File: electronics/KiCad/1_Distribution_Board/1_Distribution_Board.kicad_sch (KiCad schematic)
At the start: 10 parts, among them Q1 DMG2305UX, SW1 SW_Push

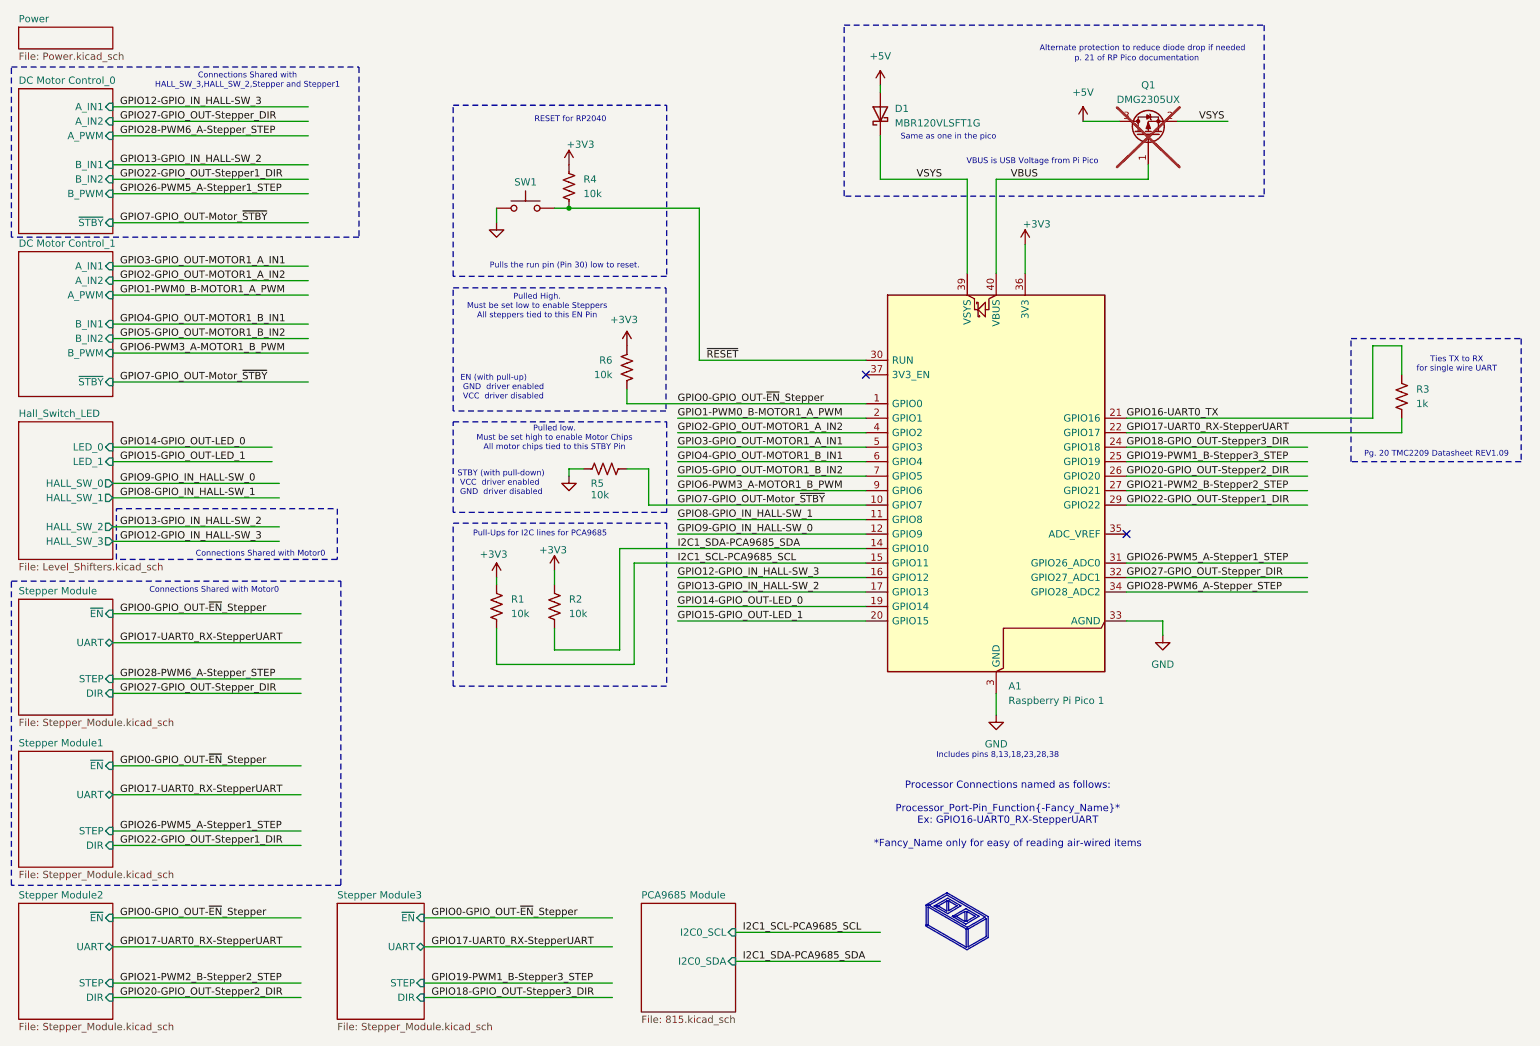
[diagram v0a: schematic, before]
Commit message: Merge board v1.3 into main (clean-clone fixups, generated files trimmed to main level) (#289)
* Initial start to updates

Removed motor pages, updated Q2,Q3, Cleaned up power module connections.

- Still need to correct routing for these updates.

* PCA Update

Updated PCA to have level shifter for I2C lines and external oscillator for precision. Corrected Power to pull from 12V.

* Removed old circuits from PCB

Removed all unused traces

* Mid work update

Lots of rework on the SCH and PCB. Checkpoint.

* Updated with more layout

Compelted PCA on board.

* adding libraries

* REV0.9 for review

Took care of all open items on the electronics PCB except for the driver resistor addresses.

* Updates Just prior to Ordering V1.0 PCBs

Updates Just prior to Ordering V1.0 PCBs

* Updates to push to V1.0

Updates to push to V1.0

* Updates to push to V1.0 missing saves. . .

Updates to push to V1.0 missing saves. . .

* Correcting Part rotation for JLCPCB

Several parts needed the "FT Rotation Offset" parameter added to correct for part orientation for JLCPCB order.

* All orientations corrected

* latest update

* Updated to reflect V1.0 of layer board as well

Updated for initial orders with PCA module populated. Also updated to layer boards for flex cables.

* Updated data and notes

* Corrected SCH for power sequence issue

5V to Vsys for all powered items.
Correction of the PCA9306 power pins.
Added decoupling to oscillator and PCA9306.

* Updated for changes to the SCH items

Updated PCB to include all changed from the SCH.

* Updated rules to correct errors

Cleaned up rules a bit to prevent false errors.

* Started work on silk update

Slowly started work on silk update.

* Corrected the 10k to 1k for connecting resistors

R1 got fixed for the correct 1k instead of 10k for UART1

* Updated Silk on PCB

Added notes for describing the pins better in the silk layer.

* Updated REV to 1.3 to reflect changes

* Updated with Version 1.3

* KiCad: make the v1.3 project 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
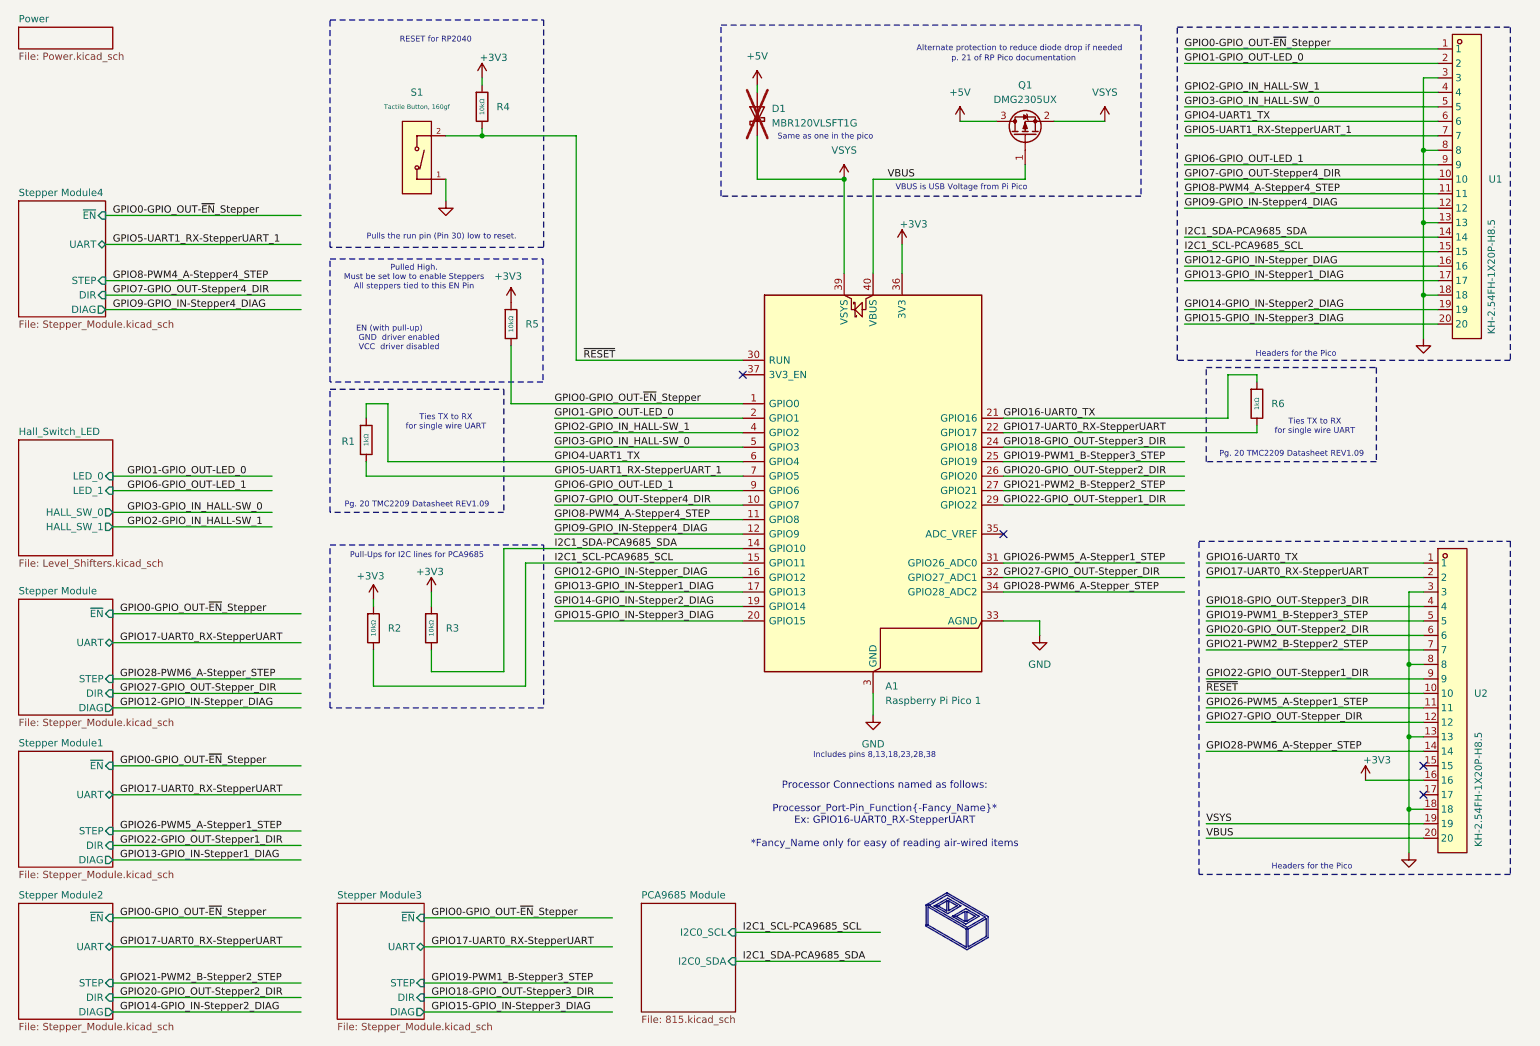
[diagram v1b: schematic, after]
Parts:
- removed R1, R2, R4, R5, R6: 10k, Resistor_SMD:R_0805_2012Metric_Pad1.20x1.40mm_HandSolder, symbol Device:R_US
- removed R3: 1k, Resistor_SMD:R_0805_2012Metric_Pad1.20x1.40mm_HandSolder, symbol Device:R_US
- removed SW1: SW_Push, Button_Switch_THT:SW_PUSH_6mm, symbol Switch:SW_Push
- added R1, R6: 1kΩ, PCM_JLCPCB:R_0603, symbol PCM_JLCPCB-Resistors:0603,1kΩ
- added R2, R3, R4, R5: 10kΩ, PCM_JLCPCB:R_0603, symbol PCM_JLCPCB-Resistors:0603,10kΩ
- added S1: Tactile Button, 160gf, PCM_JLCPCB:SW_TS-1088-AR02016, symbol PCM_JLCPCB-Connectors_Buttons:Tactile Button, 160gf, 12V, 50mA, 4.0mm
- added U1, U2: KH-2.54FH-1X20P-H8.5, EasyEDA:HDR-TH_20P-P2.54-V-F-2, symbol EasyEDA:KH-2.54FH-1X20P-H8.5
- D1: now not fitted
- Q1: LCSC (none) -> C144153; now fitted
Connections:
- net +3V3: now also R2.1, R3.1, R4.1, R5.1, U2.16
- net GND: now also S1.1 (A), U1.13, U1.18, U1.3, U1.8, U2.13, U2.18, U2.3, U2.8
- net GPIO0-GPIO_OUT-~{EN}_Stepper: now also R5.2, U1.1
- net GPIO16-UART0_TX: now also R6.1, U2.1
- net GPIO17-UART0_RX-StepperUART: now also R6.2, U2.2
- net GPIO18-GPIO_OUT-Stepper3_DIR: now also U2.4
- net GPIO19-PWM1_B-Stepper3_STEP: now also U2.5
- net GPIO20-GPIO_OUT-Stepper2_DIR: now also U2.6
- net GPIO21-PWM2_B-Stepper2_STEP: now also U2.7
- net GPIO22-GPIO_OUT-Stepper1_DIR: now also U2.9
- net GPIO26-PWM5_A-Stepper1_STEP: now also U2.11
- net GPIO27-GPIO_OUT-Stepper_DIR: now also U2.12
- net GPIO28-PWM6_A-Stepper_STEP: now also U2.14
- net I2C1_SCL-PCA9685_SCL: now also R2.2, U1.15
- net I2C1_SDA-PCA9685_SDA: now also R3.2, U1.14
- net VBUS: now also U2.20
- net VSYS: now also U2.19
- net ~{RESET}: now also R4.2, S1.2 (B), U2.10
- net GPIO1-PWM0_B-MOTOR1_A_PWM renamed GPIO1-GPIO_OUT-LED_0
- net GPIO1-GPIO_OUT-LED_0: now also U1.2
- net GPIO12-GPIO_IN_HALL-SW_3 renamed GPIO12-GPIO_IN-Stepper_DIAG
- net GPIO12-GPIO_IN-Stepper_DIAG: now also U1.16
- net GPIO13-GPIO_IN_HALL-SW_2 renamed GPIO13-GPIO_IN-Stepper1_DIAG
- net GPIO13-GPIO_IN-Stepper1_DIAG: now also U1.17
- net GPIO14-GPIO_OUT-LED_0 renamed GPIO14-GPIO_IN-Stepper2_DIAG
- net GPIO14-GPIO_IN-Stepper2_DIAG: now also U1.19
- net GPIO15-GPIO_OUT-LED_1 renamed GPIO15-GPIO_IN-Stepper3_DIAG
- net GPIO15-GPIO_IN-Stepper3_DIAG: now also U1.20
- net GPIO2-GPIO_OUT-MOTOR1_A_IN2 renamed GPIO2-GPIO_IN_HALL-SW_1
- net GPIO2-GPIO_IN_HALL-SW_1: now also U1.4
- net GPIO3-GPIO_OUT-MOTOR1_A_IN1 renamed GPIO3-GPIO_IN_HALL-SW_0
- net GPIO3-GPIO_IN_HALL-SW_0: now also U1.5
- net GPIO4-GPIO_OUT-MOTOR1_B_IN1 renamed GPIO4-UART1_TX
- net GPIO4-UART1_TX: now also R1.1, U1.6
- net GPIO5-GPIO_OUT-MOTOR1_B_IN2 renamed GPIO5-UART1_RX-StepperUART_1
- net GPIO5-UART1_RX-StepperUART_1: now also R1.2, U1.7
- net GPIO6-PWM3_A-MOTOR1_B_PWM renamed GPIO6-GPIO_OUT-LED_1
- net GPIO6-GPIO_OUT-LED_1: now also U1.9
- net GPIO7-GPIO_OUT-Motor_~{STBY} renamed GPIO7-GPIO_OUT-Stepper4_DIR
- net GPIO7-GPIO_OUT-Stepper4_DIR: now also U1.10
- net GPIO8-GPIO_IN_HALL-SW_1 renamed GPIO8-PWM4_A-Stepper4_STEP
- net GPIO8-PWM4_A-Stepper4_STEP: now also U1.11
- net GPIO9-GPIO_IN_HALL-SW_0 renamed GPIO9-GPIO_IN-Stepper4_DIAG
- net GPIO9-GPIO_IN-Stepper4_DIAG: now also U1.12
- no-connect marks 2 -> 4
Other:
- removed sheet DC Motor Control_0
- removed sheet DC Motor Control_1
- added sheet Stepper Module4 (Stepper_Module.kicad_sch)
- sheet Hall_Switch_LED ports: added none; removed HALL_SW_2, HALL_SW_3
- sheet Stepper Module ports: added DIAG; removed none
- sheet Stepper Module1 ports: added DIAG; removed none
- sheet Stepper Module2 ports: added DIAG; removed none
- sheet Stepper Module3 ports: added DIAG; removed none
- note added: "Headers for the Pico"
- note removed: "Connections Shared with HALL_SW_3,HALL_SW_2,Stepper and Stepper1"
- note removed: "Connections Shared with Motor0"
- note removed: "Pulled low. Must be set high to enable Motor Chips All motor chips tied to this STBY Pin"
- note removed: "STBY (with pull-down) VCC driver enabled GND driver disabled"
- moved on the sheet: A1
